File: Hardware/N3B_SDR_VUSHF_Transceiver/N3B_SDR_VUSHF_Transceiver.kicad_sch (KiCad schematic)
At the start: 0 parts

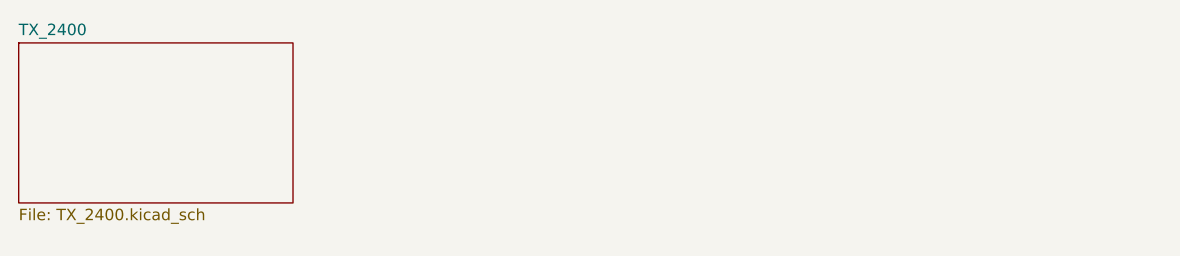
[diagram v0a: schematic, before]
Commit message: local oscillators replaced with TI
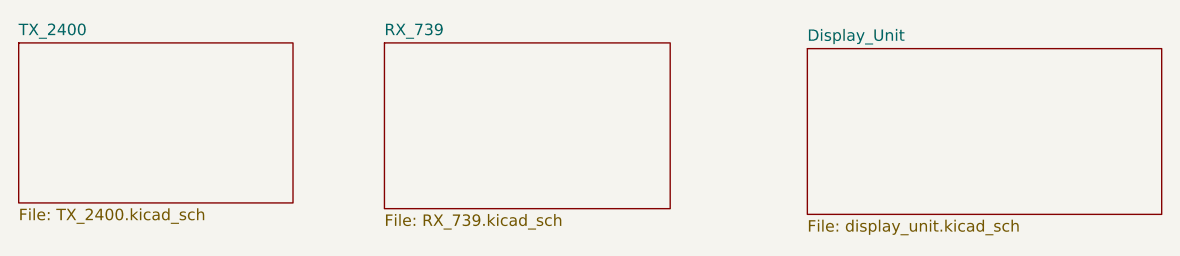
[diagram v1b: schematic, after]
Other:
- added sheet Display_Unit (display_unit.kicad_sch)
- added sheet RX_739 (RX_739.kicad_sch)
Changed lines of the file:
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@@
 	(paper "A4")
+	(sheet
+		(at 85.09 33.02)
+		(size 31.75 18.415)
+		(fields_autoplaced yes)
+		(stroke
+			(width 0.1524)
+			(type solid)
+		)
+		(fill
+			(color 0 0 0 0.0000)
+		)
+		(property "Sheetname" "RX_739"
+			(at 85.09 32.3084 0)
+			(effects
+				(font
+					(size 1.27 1.27)
+				)
+				(justify left bottom)
+			)
+		)
+		(property "Sheetfile" "RX_739.kicad_sch"
+			(at 85.09 52.0196 0)
+			(effects
+				(font
+					(size 1.27 1.27)
+				)
+				(justify left top)
+			)
+		)
+		(instances
+			(project "N3B_SDR_VUSHF_Transceiver"
+				(path "/2582416d-5e31-4efb-9478-80d896bd2c9a"
+					(page "3")
+				)
+			)
+		)
+	)
 	(sheet
 		(at 44.45 33.02)
@@
 				)
 			)
+		)
+	)
+	(sheet
+		(at 132.08 33.655)
+		(size 39.37 18.415)
+		(fields_autoplaced yes)
+		(stroke
+			(width 0.1524)
+			(type solid)
+		)
+		(fill
+			(color 0 0 0 0.0000)
+		)
+		(property "Sheetname" "Display_Unit"
+			(at 132.08 32.9434 0)
+			(effects
+				(font
+					(size 1.27 1.27)
+				)
+				(justify left bottom)
+			)
+		)
+		(property "Sheetfile" "display_unit.kicad_sch"
+			(at 132.08 52.6546 0)
+			(effects
+				(font
+					(size 1.27 1.27)
+				)
+				(justify left top)
+			)
+		)
+		(instances
+			(project "N3B_SDR_VUSHF_Transceiver"
+				(path "/2582416d-5e31-4efb-9478-80d896bd2c9a"
+					(page "4")
+				)
+			)
